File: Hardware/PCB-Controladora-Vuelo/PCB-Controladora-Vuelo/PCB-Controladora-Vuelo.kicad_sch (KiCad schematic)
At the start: 14 parts, among them J1 Jumper Serial, J2 CONN, U1 MPU-5060, U2 ESP32-DEVKIT-V1, U2 Nrf24l01, U3 AMS1117-3.3

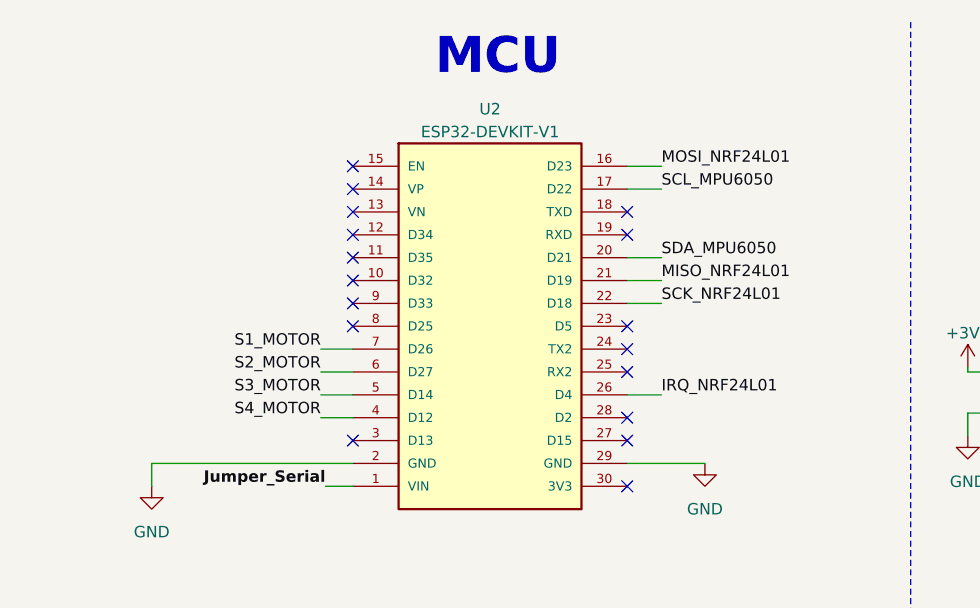
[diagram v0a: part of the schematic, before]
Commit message: Hice una mejora con un solo puente de  pista 3,3v para transeptor en donde existen riesgos pero mañana trato d mejorar y chequear pines asi se mergea
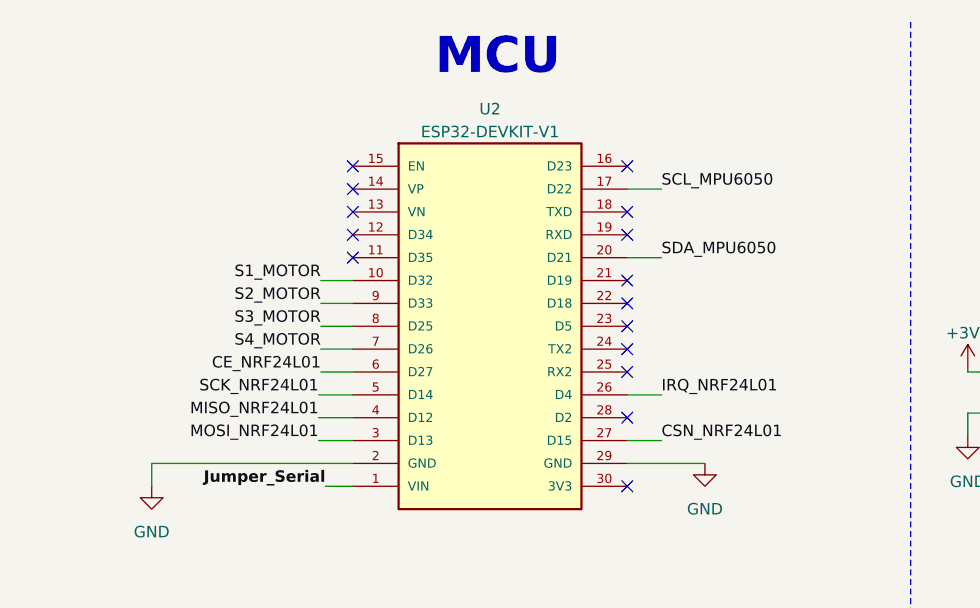
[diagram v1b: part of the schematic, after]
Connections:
- net CE_NRF24L01: now also U2.6 (D27)
- net CSN_NRF24L01: now also U2.27 (D15)
- net MISO_NRF24L01: now also U2.4 (D12); no longer U2.21 (D19)
- net MOSI_NRF24L01: now also U2.3 (D13); no longer U2.16 (D23)
- net S1_MOTOR: now also U2.10 (D32); no longer U2.7 (D26)
- net S2_MOTOR: now also U2.9 (D33); no longer U2.6 (D27)
- net S3_MOTOR: now also U2.8 (D25); no longer U2.5 (D14)
- net S4_MOTOR: now also U2.7 (D26); no longer U2.4 (D12)
- net SCK_NRF24L01: now also U2.5 (D14); no longer U2.22 (D18)
- no-connect marks 25 -> 23
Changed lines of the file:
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@@
   (junction (at 49.784 51.562) (diameter 0) (color 0 0 0 0)
   )
+  (no_connect (at 145.796 27.94))
   (no_connect (at 145.796 63.5))
   (no_connect (at 115.316 30.48))
   (no_connect (at 43.18 82.55))
+  (no_connect (at 145.796 43.18))
   (no_connect (at 115.316 35.56))
-  (no_connect (at 145.796 58.42))
-  (no_connect (at 115.316 40.64))
-  (no_connect (at 115.316 45.72))
+  (no_connect (at 145.796 40.64))
   (no_connect (at 145.796 33.02))
   (no_connect (at 115.316 38.1))
+  (no_connect (at 145.796 45.72))
   (no_connect (at 115.316 33.02))
   (no_connect (at 203.2 65.532))
   (no_connect (at 145.796 35.56))
   (no_connect (at 115.316 27.94))
-  (no_connect (at 115.316 43.18))
   (no_connect (at 145.796 55.88))
   (no_connect (at 203.2 68.072))
@@
   (no_connect (at 43.18 110.49))
   (no_connect (at 203.2 70.612))
-  (no_connect (at 145.796 45.72))
-  (no_connect (at 115.316 58.42))
   (no_connect (at 145.796 48.26))
   (no_connect (at 145.796 50.8))
@@
     (stroke (width 0) (type default))
   )
+  (wire (pts (xy 115.316 55.88) (xy 111.506 55.88))
+    (stroke (width 0) (type default))
+  )
   (wire (pts (xy 149.606 38.1) (xy 145.796 38.1))
     (stroke (width 0) (type default))
@@
     (stroke (width 0) (type default))
   )
+  (wire (pts (xy 111.76 45.72) (xy 115.316 45.72))
+    (stroke (width 0) (type default))
+  )
   (wire (pts (xy 145.796 53.34) (xy 149.606 53.34))
     (stroke (width 0) (type default))
@@
     (stroke (width 0) (type default))
   )
+  (wire (pts (xy 111.76 50.8) (xy 115.316 50.8))
+    (stroke (width 0) (type default))
+  )
   (polyline (pts (xy 71.12 11.938) (xy 71.12 73.66))
     (stroke (width 0) (type dash))
   )
-  (wire (pts (xy 111.76 50.8) (xy 115.316 50.8))
+  (wire (pts (xy 57.658 46.482) (xy 57.658 51.562))
     (stroke (width 0) (type default))
   )
-  (wire (pts (xy 57.658 46.482) (xy 57.658 51.562))
+  (wire (pts (xy 115.316 53.34) (xy 111.506 53.34))
     (stroke (width 0) (type default))
   )
@@
     (stroke (width 0) (type default))
   )
-  (wire (pts (xy 145.796 40.64) (xy 149.606 40.64))
-    (stroke (width 0) (type default))
-  )
   (wire (pts (xy 230.886 134.112) (xy 230.886 136.652))
     (stroke (width 0) (type default))
@@
     (stroke (width 0) (type default))
   )
-  (wire (pts (xy 111.76 48.26) (xy 115.316 48.26))
-    (stroke (width 0) (type default))
-  )
   (wire (pts (xy 183.642 50.8) (xy 203.2 50.8))
     (stroke (width 0) (type default))
@@
     (stroke (width 0) (type default))
   )
+  (wire (pts (xy 115.316 58.42) (xy 111.506 58.42))
+    (stroke (width 0) (type default))
+  )
   (wire (pts (xy 33.02 85.09) (xy 43.18 85.09))
     (stroke (width 0) (type default))
@@
     (stroke (width 0) (type default))
   )
+  (wire (pts (xy 111.76 40.64) (xy 115.316 40.64))
+    (stroke (width 0) (type default))
+  )
   (wire (pts (xy 49.784 51.562) (xy 57.658 51.562))
     (stroke (width 0) (type default))
@@
     (stroke (width 0) (type default))
   )
-  (wire (pts (xy 111.76 55.88) (xy 115.316 55.88))
-    (stroke (width 0) (type default))
-  )
-  (wire (pts (xy 145.796 43.18) (xy 149.606 43.18))
+  (wire (pts (xy 111.76 48.26) (xy 115.316 48.26))
     (stroke (width 0) (type default))
   )
@@
     (stroke (width 0) (type default))
   )
-  (wire (pts (xy 111.76 53.34) (xy 115.316 53.34))
-    (stroke (width 0) (type default))
-  )
   (polyline (pts (xy 177.292 84.582) (xy 284.988 84.582))
     (stroke (width 0) (type dash))
   )
-  (wire (pts (xy 145.796 27.94) (xy 149.606 27.94))
+  (wire (pts (xy 149.606 58.42) (xy 145.796 58.42))
     (stroke (width 0) (type default))
   )
@@
     (stroke (width 0) (type default))
   )
+  (wire (pts (xy 111.76 43.18) (xy 115.316 43.18))
+    (stroke (width 0) (type default))
+  )
   (wire (pts (xy 203.2 50.8) (xy 203.2 52.832))
     (stroke (width 0) (type default))
@@
     (effects (font (size 1.27 1.27)) (justify right bottom))
   )
-  (label "S3_MOTOR" (at 111.76 53.34 180) (fields_autoplaced)
-    (effects (font (size 1.27 1.27)) (justify right bottom))
-  )
-  (label "MISO_NRF24L01" (at 149.606 40.64 0) (fields_autoplaced)
-    (effects (font (size 1.27 1.27)) (justify left bottom))
-  )
   (label "IRQ_NRF24L01" (at 149.606 53.34 0) (fields_autoplaced)
     (effects (font (size 1.27 1.27)) (justify left bottom))
   )
-  (label "S4_MOTOR" (at 111.76 55.88 180) (fields_autoplaced)
-    (effects (font (size 1.27 1.27)) (justify right bottom))
-  )
-  (label "S1_MOTOR" (at 111.76 48.26 180) (fields_autoplaced)
-    (effects (font (size 1.27 1.27)) (justify right bottom))
-  )
   (label "MISO_NRF24L01" (at 213.106 125.222 180) (fields_autoplaced)
     (effects (font (size 1.27 1.27)) (justify right bottom))
@@
     (effects (font (size 1.27 1.27)) (justify left bottom))
   )
+  (label "MOSI_NRF24L01" (at 111.506 58.42 180) (fields_autoplaced)
+    (effects (font (size 1.27 1.27)) (justify right bottom))
+  )
   (label "SCL_MPU6050" (at 199.644 57.912 180) (fields_autoplaced)
     (effects (font (size 1.27 1.27)) (justify right bottom))
   )
-  (label "SCK_NRF24L01" (at 149.606 43.18 0) (fields_autoplaced)
+  (label "CSN_NRF24L01" (at 149.606 58.42 0) (fields_autoplaced)
     (effects (font (size 1.27 1.27)) (justify left bottom))
   )
+  (label "S3_MOTOR" (at 111.76 45.72 180) (fields_autoplaced)
+    (effects (font (size 1.27 1.27)) (justify right bottom))
+  )
   (label "MOSI_NRF24L01" (at 213.106 122.682 180) (fields_autoplaced)
     (effects (font (size 1.27 1.27)) (justify right bottom))
@@
     (effects (font (size 1.27 1.27) bold) (justify right bottom))
   )
-  (label "MOSI_NRF24L01" (at 149.606 27.94 0) (fields_autoplaced)
-    (effects (font (size 1.27 1.27)) (justify left bottom))
+  (label "S4_MOTOR" (at 111.76 48.26 180) (fields_autoplaced)
+    (effects (font (size 1.27 1.27)) (justify right bottom))
   )
   (label "SCK_NRF24L01" (at 213.106 120.142 180) (fields_autoplaced)
     (effects (font (size 1.27 1.27)) (justify right bottom))
   )
-  (label "S2_MOTOR" (at 111.76 50.8 180) (fields_autoplaced)
+  (label "S3_MOTOR" (at 39.37 102.87 180) (fields_autoplaced)
     (effects (font (size 1.27 1.27)) (justify right bottom))
   )
-  (label "S3_MOTOR" (at 39.37 102.87 180) (fields_autoplaced)
+  (label "S2_MOTOR" (at 111.76 43.18 180) (fields_autoplaced)
     (effects (font (size 1.27 1.27)) (justify right bottom))
   )
@@
     (effects (font (size 1.27 1.27)) (justify right bottom))
   )
+  (label "CE_NRF24L01" (at 111.76 50.8 180) (fields_autoplaced)
+    (effects (font (size 1.27 1.27)) (justify right bottom))
+  )
+  (label "MISO_NRF24L01" (at 111.506 55.88 180) (fields_autoplaced)
+    (effects (font (size 1.27 1.27)) (justify right bottom))
+  )
   (label "SCL_MPU6050" (at 149.606 30.48 0) (fields_autoplaced)
     (effects (font (size 1.27 1.27)) (justify left bottom))
   )
+  (label "S1_MOTOR" (at 111.76 40.64 180) (fields_autoplaced)
+    (effects (font (size 1.27 1.27)) (justify right bottom))
+  )
   (label "S1_MOTOR" (at 39.37 97.79 180) (fields_autoplaced)
     (effects (font (size 1.27 1.27)) (justify right bottom))
   )
+  (label "SCK_NRF24L01" (at 111.506 53.34 180) (fields_autoplaced)
+    (effects (font (size 1.27 1.27)) (justify right bottom))
+  )

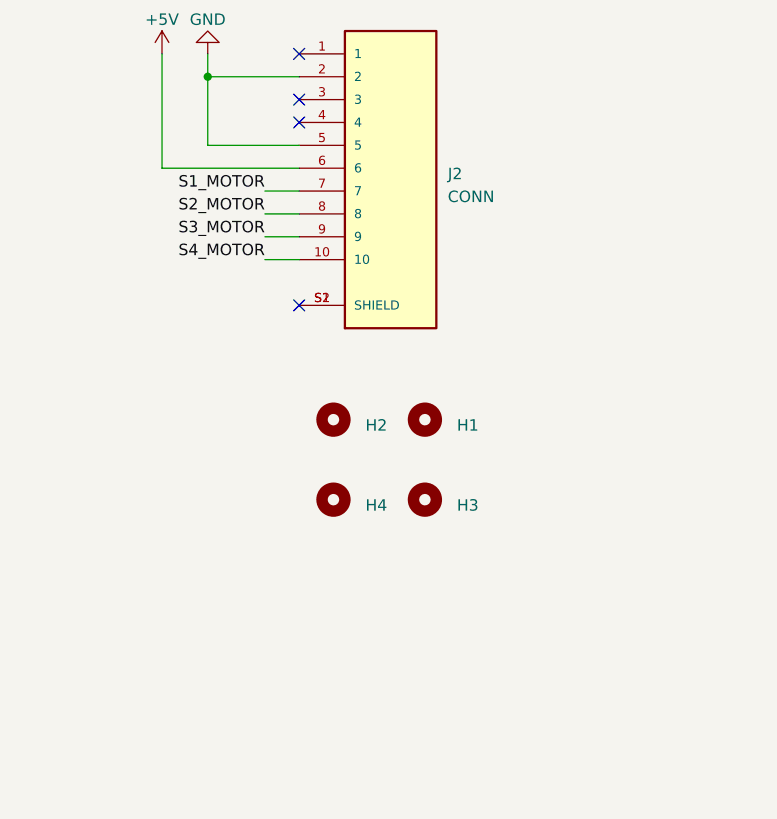
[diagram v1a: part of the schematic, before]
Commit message: MODIFIQUE ESQUEMATICO Y PCB FINALIZADO DIRIA yo falta aprobacion de legui lo deje con 2 puentes para mas seguridad , nuevo puente pin MOSI NRF24L01 Y PLACA LISTA CHEQUEO EL 3D Y VAVVAVVAVA
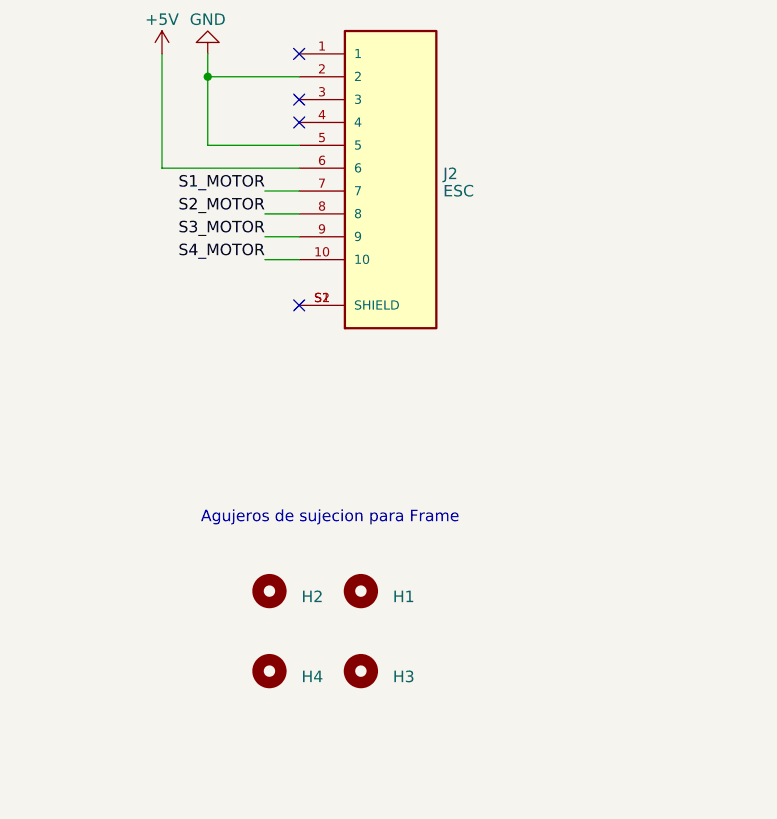
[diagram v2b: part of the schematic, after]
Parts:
- J2: value CONN -> ESC
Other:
- note added: "Agujeros de sujecion para Frame"
- moved on the sheet: H1, H2, H3, H4
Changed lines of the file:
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@@
     (effects (font (size 4 4) (thickness 0.8) bold) (justify left bottom))
+  )
+  (text "Agujeros de sujecion para Frame\n" (at 32.258 134.874 0)
+    (effects (font (size 1.27 1.27)) (justify left bottom))
   )
   (text "Alimentación\n" (at 21.336 22.098 0)
@@
   (symbol (lib_id "Librerias:JST-1mm") (at 53.34 95.25 0) (unit 1)
     (in_bom yes) (on_board yes) (dnp no) (fields_autoplaced)
-    (property "Reference" "J2" (at 59.69 95.885 0)
-      (effects (font (size 1.27 1.27)) (justify left))
-    )
-    (property "Value" "CONN" (at 59.69 98.425 0)
+    (property "Reference" "J2" (at 59.182 95.8763 0)
+      (effects (font (size 1.27 1.27)) (justify left))
+    )
+    (property "Value" "ESC" (at 59.182 97.7973 0)
       (effects (font (size 1.27 1.27)) (justify left))
     )
@@
     )
   )
-  (symbol (lib_id "EESTN5:Mounting_Hole") (at 46.99 123.19 0) (unit 1)
-    (in_bom yes) (on_board yes) (dnp no) (fields_autoplaced)
-    (property "Reference" "H2" (at 50.546 123.825 0)
-      (effects (font (size 1.27 1.27)) (justify left))
-    )
-    (property "Value" "Mounting_Hole" (at 46.99 120.015 0)
-      (effects (font (size 1.27 1.27)) hide)
-    )
-    (property "Footprint" "EESTN5:hole_3mm" (at 46.99 123.19 0)
-      (effects (font (size 1.524 1.524)) hide)
-    )
-    (property "Datasheet" "" (at 46.99 123.19 0)
+  (symbol (lib_id "EESTN5:Mounting_Hole") (at 39.878 142.24 0) (unit 1)
+    (in_bom yes) (on_board yes) (dnp no) (fields_autoplaced)
+    (property "Reference" "H2" (at 43.434 142.875 0)
+      (effects (font (size 1.27 1.27)) (justify left))
+    )
+    (property "Value" "Mounting_Hole" (at 39.878 139.065 0)
+      (effects (font (size 1.27 1.27)) hide)
+    )
+    (property "Footprint" "EESTN5:hole_3mm" (at 39.878 142.24 0)
+      (effects (font (size 1.524 1.524)) hide)
+    )
+    (property "Datasheet" "" (at 39.878 142.24 0)
       (effects (font (size 1.524 1.524)) hide)
     )
@@
     )
   )
-  (symbol (lib_id "EESTN5:Mounting_Hole") (at 57.15 123.19 0) (unit 1)
-    (in_bom yes) (on_board yes) (dnp no) (fields_autoplaced)
-    (property "Reference" "H1" (at 60.706 123.825 0)
-      (effects (font (size 1.27 1.27)) (justify left))
-    )
-    (property "Value" "Mounting_Hole" (at 57.15 120.015 0)
-      (effects (font (size 1.27 1.27)) hide)
-    )
-    (property "Footprint" "EESTN5:hole_3mm" (at 57.15 123.19 0)
-      (effects (font (size 1.524 1.524)) hide)
-    )
-    (property "Datasheet" "" (at 57.15 123.19 0)
+  (symbol (lib_id "EESTN5:Mounting_Hole") (at 50.038 142.24 0) (unit 1)
+    (in_bom yes) (on_board yes) (dnp no) (fields_autoplaced)
+    (property "Reference" "H1" (at 53.594 142.875 0)
+      (effects (font (size 1.27 1.27)) (justify left))
+    )
+    (property "Value" "Mounting_Hole" (at 50.038 139.065 0)
+      (effects (font (size 1.27 1.27)) hide)
+    )
+    (property "Footprint" "EESTN5:hole_3mm" (at 50.038 142.24 0)
+      (effects (font (size 1.524 1.524)) hide)
+    )
+    (property "Datasheet" "" (at 50.038 142.24 0)
       (effects (font (size 1.524 1.524)) hide)
     )
@@
     )
   )
-  (symbol (lib_id "EESTN5:Mounting_Hole") (at 46.99 132.08 0) (unit 1)
-    (in_bom yes) (on_board yes) (dnp no) (fields_autoplaced)
-    (property "Reference" "H4" (at 50.546 132.715 0)
-      (effects (font (size 1.27 1.27)) (justify left))
-    )
-    (property "Value" "Mounting_Hole" (at 46.99 128.905 0)
-      (effects (font (size 1.27 1.27)) hide)
-    )
-    (property "Footprint" "EESTN5:hole_3mm" (at 46.99 132.08 0)
-      (effects (font (size 1.524 1.524)) hide)
-    )
-    (property "Datasheet" "" (at 46.99 132.08 0)
+  (symbol (lib_id "EESTN5:Mounting_Hole") (at 39.878 151.13 0) (unit 1)
+    (in_bom yes) (on_board yes) (dnp no) (fields_autoplaced)
+    (property "Reference" "H4" (at 43.434 151.765 0)
+      (effects (font (size 1.27 1.27)) (justify left))
+    )
+    (property "Value" "Mounting_Hole" (at 39.878 147.955 0)
+      (effects (font (size 1.27 1.27)) hide)
+    )
+    (property "Footprint" "EESTN5:hole_3mm" (at 39.878 151.13 0)
+      (effects (font (size 1.524 1.524)) hide)
+    )
+    (property "Datasheet" "" (at 39.878 151.13 0)
       (effects (font (size 1.524 1.524)) hide)
     )
@@
     )
   )
-  (symbol (lib_id "EESTN5:Mounting_Hole") (at 57.15 132.08 0) (unit 1)
-    (in_bom yes) (on_board yes) (dnp no) (fields_autoplaced)
-    (property "Reference" "H3" (at 60.706 132.715 0)
-      (effects (font (size 1.27 1.27)) (justify left))
-    )
-    (property "Value" "Mounting_Hole" (at 57.15 128.905 0)
-      (effects (font (size 1.27 1.27)) hide)
-    )
-    (property "Footprint" "EESTN5:hole_3mm" (at 57.15 132.08 0)
-      (effects (font (size 1.524 1.524)) hide)
-    )
-    (property "Datasheet" "" (at 57.15 132.08 0)
-      (effects (font (size 1.524 1.524)) hide)
-    )
+  (symbol (lib_id "EESTN5:Mounting_Hole") (at 50.038 151.13 0) (unit 1)
+    (in_bom yes) (on_board yes) (dnp no) (fields_autoplaced)
+    (property "Reference" "H3" (at 53.594 151.765 0)
+      (effects (font (size 1.27 1.27)) (justify left))
+    )
+    (property "Value" "Mounting_Hole" (at 50.038 147.955 0)
+      (effects (font (size 1.27 1.27)) hide)
+    )
+    (property "Footprint" "EESTN5:hole_3mm" (at 50.038 151.13 0)
+      (effects (font (size 1.524 1.524)) hide)
+    )
+    (property "Datasheet" "" (at 50.038 151.13 0)
+      (effects (font (size 1.524 1.524)) hide)
+    )

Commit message: Cambie capacitores y agregue componentes smd , quedo bien cambie los capacitores electroliticos , queda duda de la huella jst y el posicionamiento de los agujeros de sujecion y ajustar la placa a un tamaño comodo
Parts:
- C5, C7: footprint Capacitor_SMD:C_1206_3216Metric -> Capacitor_THT:CP_Radial_D4.0mm_P1.50mm
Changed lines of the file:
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@@
       (effects (font (size 1.27 1.27)) (justify left))
     )
-    (property "Footprint" "Capacitor_SMD:C_1206_3216Metric" (at 50.7492 60.452 0)
+    (property "Footprint" "Capacitor_THT:CP_Radial_D4.0mm_P1.50mm" (at 50.7492 60.452 0)
       (effects (font (size 1.27 1.27)) hide)
     )
@@
       (effects (font (size 1.27 1.27)) (justify left))
     )
-    (property "Footprint" "Capacitor_SMD:C_1206_3216Metric" (at 23.0632 60.452 0)
-      (effects (font (size 1.27 1.27)) hide)
-    )
+    (property "Footprint" "Capacitor_THT:CP_Radial_D4.0mm_P1.50mm" (at 23.0632 60.452 0)
+      (effects (font (size 1.27 1.27)) hide)
+    )
